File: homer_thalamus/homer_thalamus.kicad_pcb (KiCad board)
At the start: 4 copper layers, 95 x 56 mm, 24 parts, among them J1 GPIO, J2 MotDrv_Pow_Conn, J3 Right_Motor_Conn, J4 Left_Motor_Conn, J5 Spare_GP_Conn, J6 VBUS_Conn, SW1 SW_PULLDOWN, U1 DRV8874_CARRIER_RIGHT, U2 DRV8874_CARRIER_LEFT, U3 HC-SR04, U4 HiLetGo-GY-521

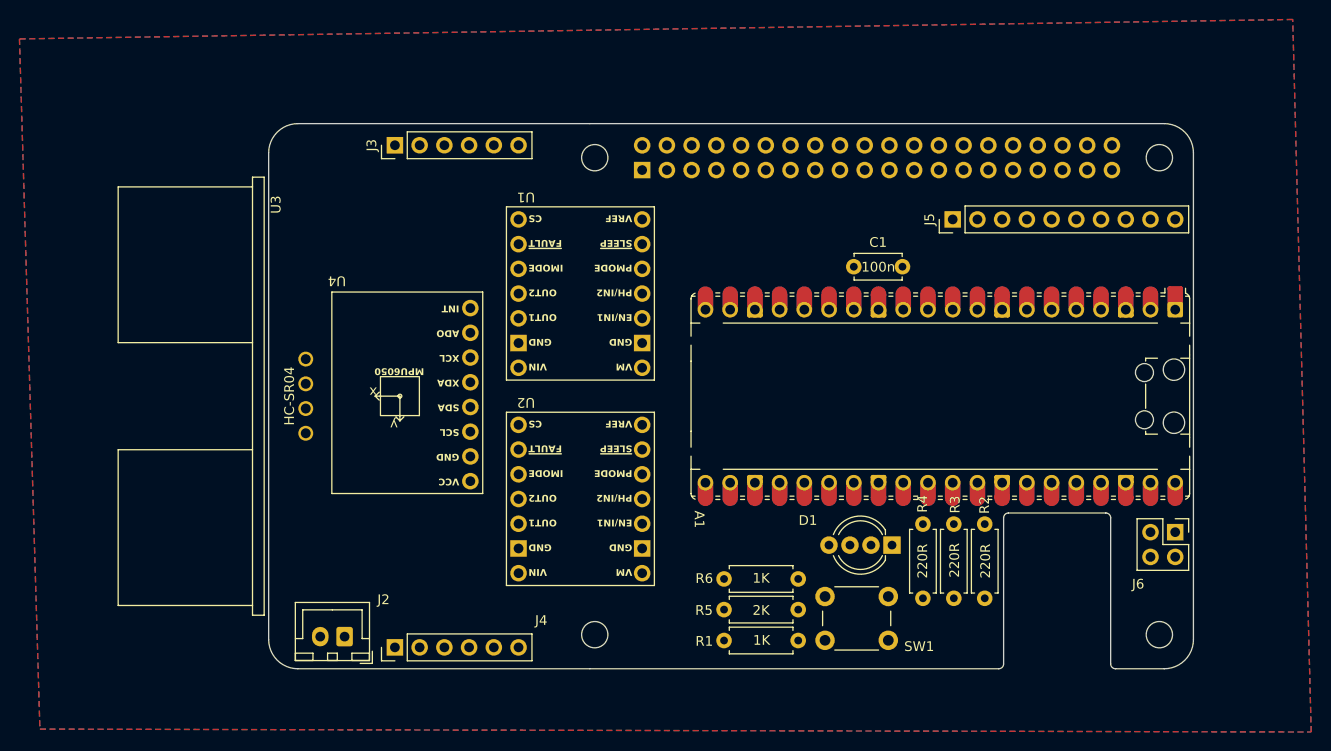
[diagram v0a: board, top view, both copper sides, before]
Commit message: route pcb tracks
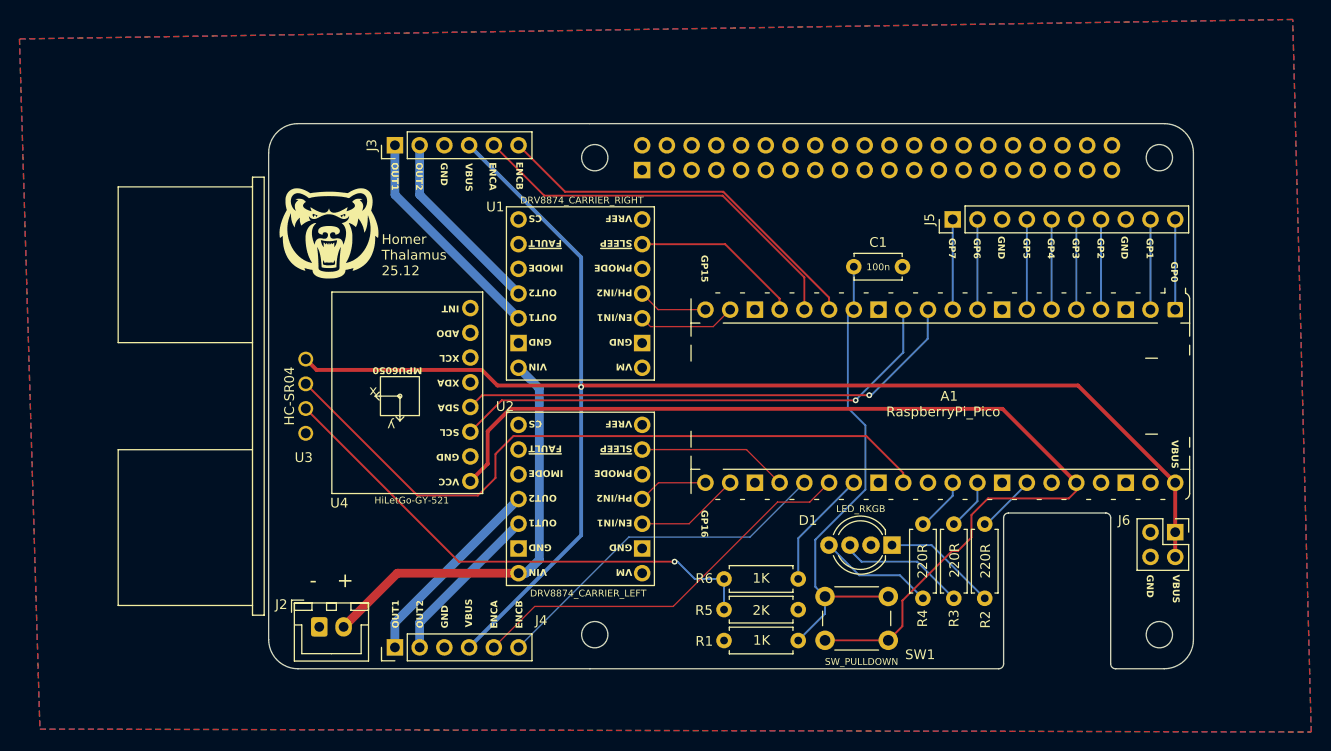
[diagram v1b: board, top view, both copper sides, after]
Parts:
- added G***: LOGO, LOGO, F.Cu at (76.2, 55.3)
- A1: footprint Module:RaspberryPi_Pico_Common_Unspecified -> RaspberryPi_Pico_THT:RaspberryPi_Pico_THT
- moved J2 2.79 mm to (75.2, 95.7), turned to 0 degrees
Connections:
- A1 pad 19: /PH_R -> /EN_R
- A1 pad 20: /EN_R -> /PH_R
- A1 pad 21: /~{SLP}_L -> /PH_L
- A1 pad 22: /PH_L -> /EN_L
- A1 pad 24: /EN_L -> /~{SLP}_L
- J2 pad 1: VMOT -> GND
- J2 pad 2: GND -> VMOT
- J4 pad 5: /ENCB_L -> /ENCA_L
- J4 pad 6: /ENCA_L -> /ENCB_L
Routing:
- net VBUS: track 0.00 -> 163.4 mm, vias 0 -> 1
- net 3V3(OUT): track 0.00 -> 106.3 mm
- net /TRIG: track 0.00 -> 72.7 mm
- net Net-(U3-ECHO): track 0.00 -> 53.4 mm, vias 0 -> 1
- net /I2C0_SDA: track 0.00 -> 52.9 mm, vias 0 -> 1
- net /I2C0_SCL: track 0.00 -> 52.3 mm, vias 0 -> 1
- net /SW_PD: track 0.00 -> 49.6 mm
- net VMOT: track 0.00 -> 43.6 mm
- net /ENCA_L: track 0.00 -> 41.4 mm
- net /ENCA_R: track 0.00 -> 40.8 mm
- net /ENCB_R: track 0.00 -> 39.6 mm
- net /ENCB_L: track 0.00 -> 36.4 mm
- net /OUT1_R: track 0.00 -> 23.0 mm
- net /OUT2_L: track 0.00 -> 20.5 mm
- net /OUT2_R: track 0.00 -> 19.4 mm
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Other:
- board text added: "+"
- board text added: "-"
- board text added: "ENCA"
- board text added: "ENCB"
- board text added: "GND"
- board text added: "GP1"
- board text added: "GP2"
- board text added: "GP3"
- board text added: "GP4"
- board text added: "GP5"
- board text added: "GP6"
- board text added: "GP7"
- board text added: "Homer Thalamus 25.12"
- board text added: "OUT1"
- board text added: "OUT2"
- board text added: "VBUS"

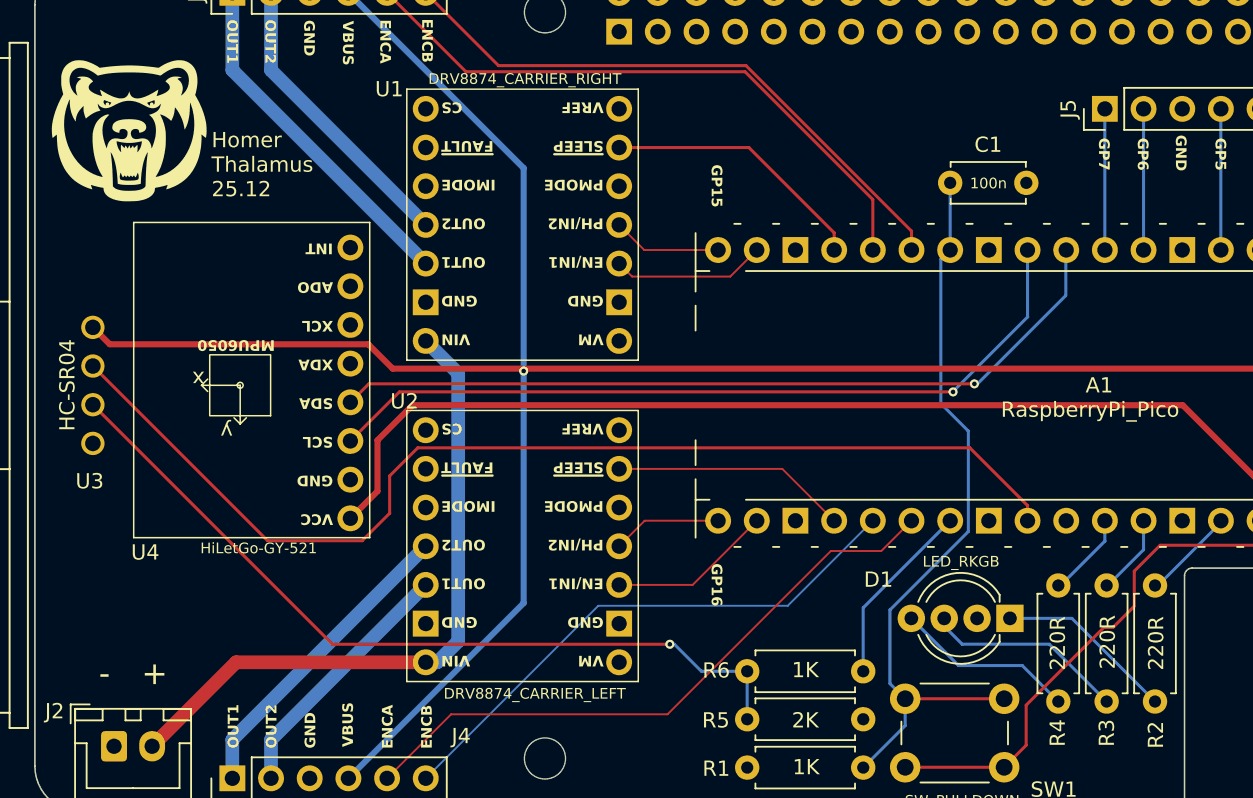
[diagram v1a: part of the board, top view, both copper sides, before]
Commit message: add GY521 mounting and 3d model
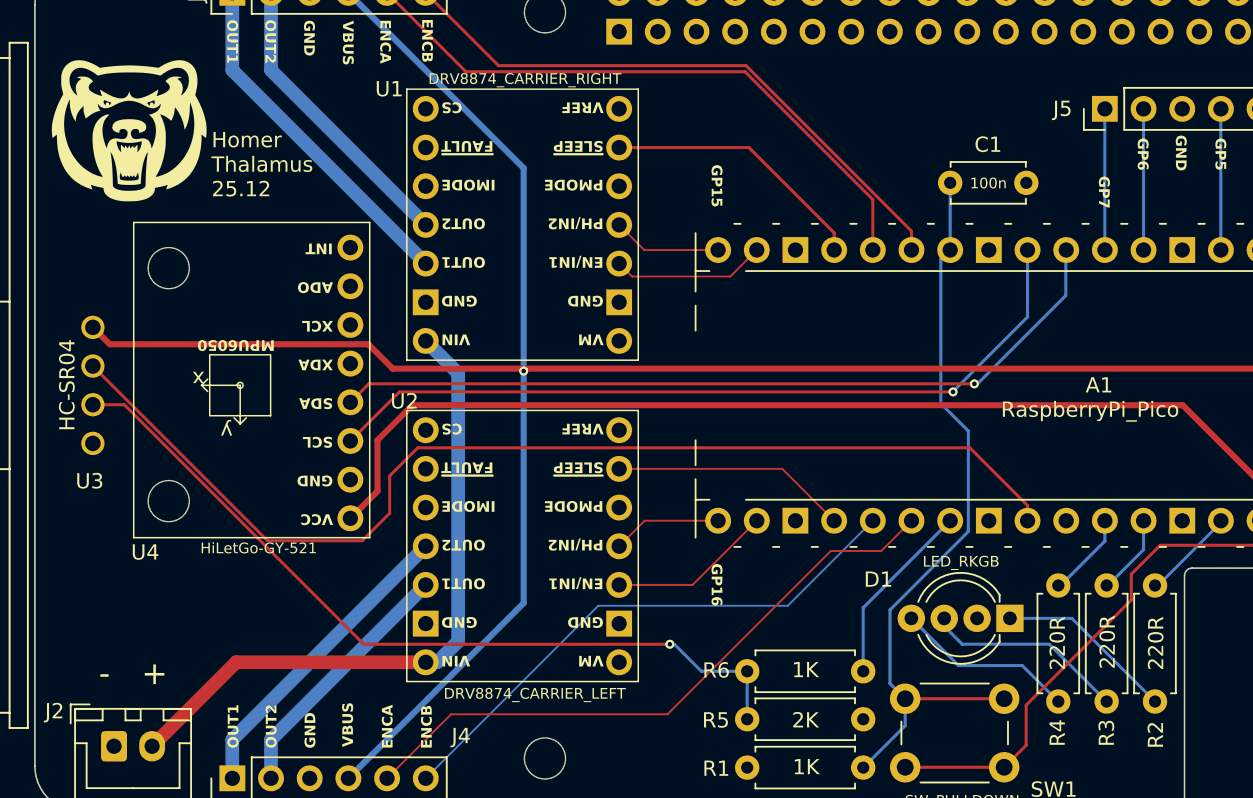
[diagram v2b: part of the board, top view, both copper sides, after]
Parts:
- added ?: , , F.Cu at (78.8, 64.3)
- added ?: , , F.Cu at (78.8, 79.6)
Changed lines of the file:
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@@
 		)
 	)
+	(footprint ""
+		(layer "F.Cu")
+		(at 78.79 64.3)
+		(property "Reference" ""
+			(at 0 0 0)
+			(layer "F.SilkS")
+			(effects
+				(font
+					(size 1.27 1.27)
+					(thickness 0.15)
+				)
+			)
+		)
+		(property "Value" ""
+			(at 0 0 0)
+			(layer "F.Fab")
+			(effects
+				(font
+					(size 1.27 1.27)
+					(thickness 0.15)
+				)
+			)
+		)
+		(property "Datasheet" ""
+			(at 0 0 0)
+			(layer "F.Fab")
+			(hide yes)
+			(effects
+				(font
+					(size 1.27 1.27)
+					(thickness 0.15)
+				)
+			)
+		)
+		(property "Description" ""
+			(at 0 0 0)
+			(layer "F.Fab")
+			(hide yes)
+			(effects
+				(font
+					(size 1.27 1.27)
+					(thickness 0.15)
+				)
+			)
+		)
+		(pad "" np_thru_hole circle
+			(at 0 0)
+			(size 2.7 2.7)
+			(drill 2.7)
+			(layers "*.Cu" "*.Mask")
+		)
+		(embedded_fonts no)
+	)
 	(footprint "MountingHole:MountingHole_2.7mm_M2.5"
 		(locked yes)
@@
 		)
 		(embedded_fonts no)
+		(model "${KIPRJMOD}/GY-521/GY-521_MPU6050 Accelerometer.step"
+			(offset
+				(xyz -0.5 0 5)
+			)
+			(scale
+				(xyz 1 1 1)
+			)
+			(rotate
+				(xyz -0 -0 90)
+			)
+		)
 	)
 	(footprint "MountingHole:MountingHole_2.7mm_M2.5"
@@
 		(embedded_fonts no)
 	)
+	(footprint ""
+		(layer "F.Cu")
+		(at 78.79 79.6)
+		(property "Reference" ""
+			(at 0 0 0)
+			(layer "F.SilkS")
+			(effects
+				(font
+					(size 1.27 1.27)
+					(thickness 0.15)
+				)
+			)
+		)
+		(property "Value" ""
+			(at 0 0 0)
+			(layer "F.Fab")
+			(effects
+				(font
+					(size 1.27 1.27)
+					(thickness 0.15)
+				)
+			)
+		)
+		(property "Datasheet" ""
+			(at 0 0 0)
+			(layer "F.Fab")
+			(hide yes)
+			(effects
+				(font
+					(size 1.27 1.27)
+					(thickness 0.15)
+				)
+			)
+		)
+		(property "Description" ""
+			(at 0 0 0)
+			(layer "F.Fab")
+			(hide yes)
+			(effects
+				(font
+					(size 1.27 1.27)
+					(thickness 0.15)
+				)
+			)
+		)
+		(pad "" np_thru_hole circle
+			(at 0 0)
+			(size 2.7 2.7)
+			(drill 2.7)
+			(layers "*.Cu" "*.Mask")
+		)
+		(embedded_fonts no)
+	)
 	(footprint "MountingHole:MountingHole_2.7mm_M2.5"
 		(locked yes)
@@
 		(tags "Through hole pin header THT 1x10 2.54mm single row")
 		(property "Reference" "J5"
-			(at 0 -2.38 90)
+			(at 0 -2.77 180)
 			(layer "F.SilkS")
 			(effects
@@
 	)
 	(gr_text "GP7"
-		(at 139.8 57.9 270)
+		(at 139.8 60.4 270)
 		(layer "F.SilkS")
 		(effects
@@
 	)
 	(segment
-		(start 143.9 82.5)
-		(end 152.2 82.5)
+		(start 152.2 82.5)
+		(end 152.97 81.73)
 		(width 0.2)
 		(layer "F.Cu")
@@
 	)
 	(segment
-		(start 135.1 95.634)
-		(end 135.1 93)
+		(start 142 84.4)
+		(end 143.9 82.5)
 		(width 0.2)
 		(layer "F.Cu")
@@
 	)
 	(segment
-		(start 152.2 82.5)
-		(end 152.97 81.73)
+		(start 142 86.1)
+		(end 142 84.4)
 		(width 0.2)
 		(layer "F.Cu")
@@
 	)
 	(segment
-		(start 152.97 81.73)
-		(end 152.97 80.89)
+		(start 143.9 82.5)
+		(end 152.2 82.5)
+		(width 0.2)
+		(layer "F.Cu")
+		(net 35)
+	)
+	(segment
+		(start 135.1 95.634)
+		(end 135.1 93)
 		(width 0.2)
 		(layer "F.Cu")
@@
 	)
 	(segment
-		(start 133.655 97.079)
-		(end 135.1 95.634)
-		(width 0.2)
-		(layer "F.Cu")
-		(net 35)
-	)
-	(segment
-		(start 140.2 87.9)
-		(end 140.8 87.9)
-		(width 0.2)
-		(layer "F.Cu")
-		(net 35)
-	)
-	(segment
-		(start 140.8 87.9)
-		(end 142.2 86.5)
+		(start 152.97 81.73)
+		(end 152.97 80.89)
 		(width 0.2)
 		(layer "F.Cu")
@@
 	)
 	(segment
-		(start 142.2 86.5)
-		(end 142.2 84.2)
+		(start 135.1 93)
+		(end 142 86.1)
 		(width 0.2)
 		(layer "F.Cu")
@@
 	)
 	(segment
-		(start 142.2 84.2)
-		(end 143.9 82.5)
-		(width 0.2)
-		(layer "F.Cu")
-		(net 35)
-	)
-	(segment
 		(start 92.5 75.6)
 		(end 94.8 73.3)
@@
 	)
 	(segment
-		(start 135.1 93)
-		(end 140.2 87.9)
+		(start 133.655 97.079)
+		(end 135.1 95.634)
 		(width 0.2)
 		(layer "F.Cu")
@@
 	)
 	(segment
+		(start 91.6 89)
+		(end 111.7 89)
+		(width 0.2)
+		(layer "F.Cu")
+		(net 72)
+	)
+	(segment
 		(start 73.81 73.27)
-		(end 89.54 89)
+		(end 75.87 73.27)
 		(width 0.2)
 		(layer "F.Cu")
@@
 	)
 	(segment
-		(start 89.54 89)
-		(end 111.7 89)
+		(start 75.87 73.27)
+		(end 91.6 89)
 		(width 0.2)
 		(layer "F.Cu")
